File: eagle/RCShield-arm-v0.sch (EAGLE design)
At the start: 48 parts, among them U3 TS5A3157DBV, U4 XBEE, U5 TS5A3157DBV, X1 USB

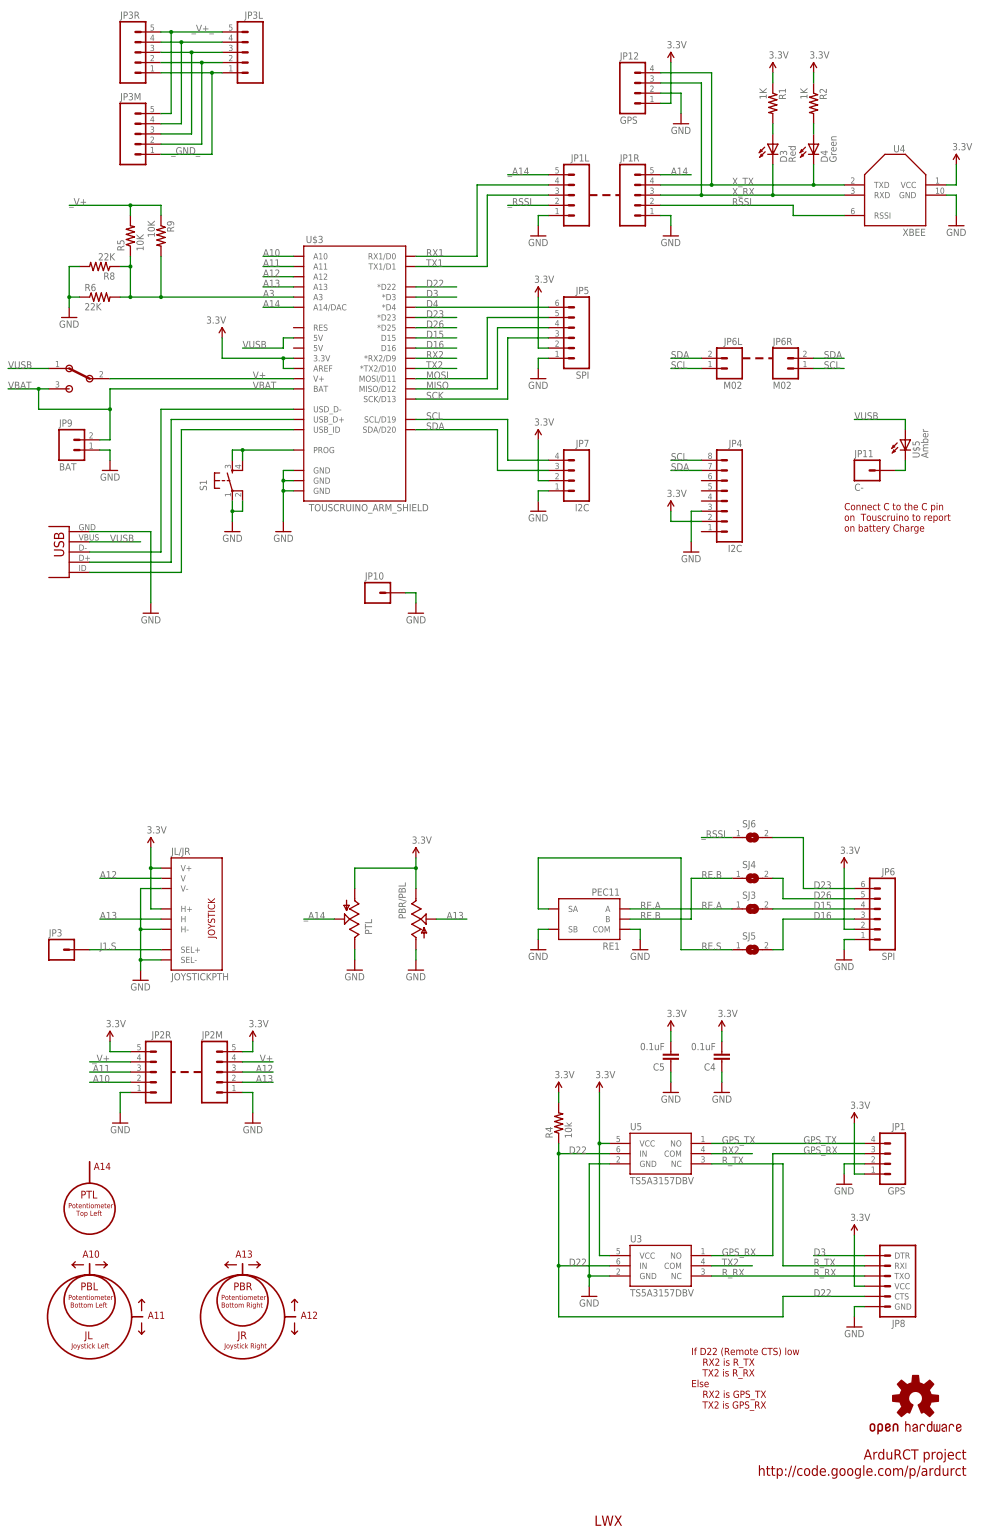
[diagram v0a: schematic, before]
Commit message: 
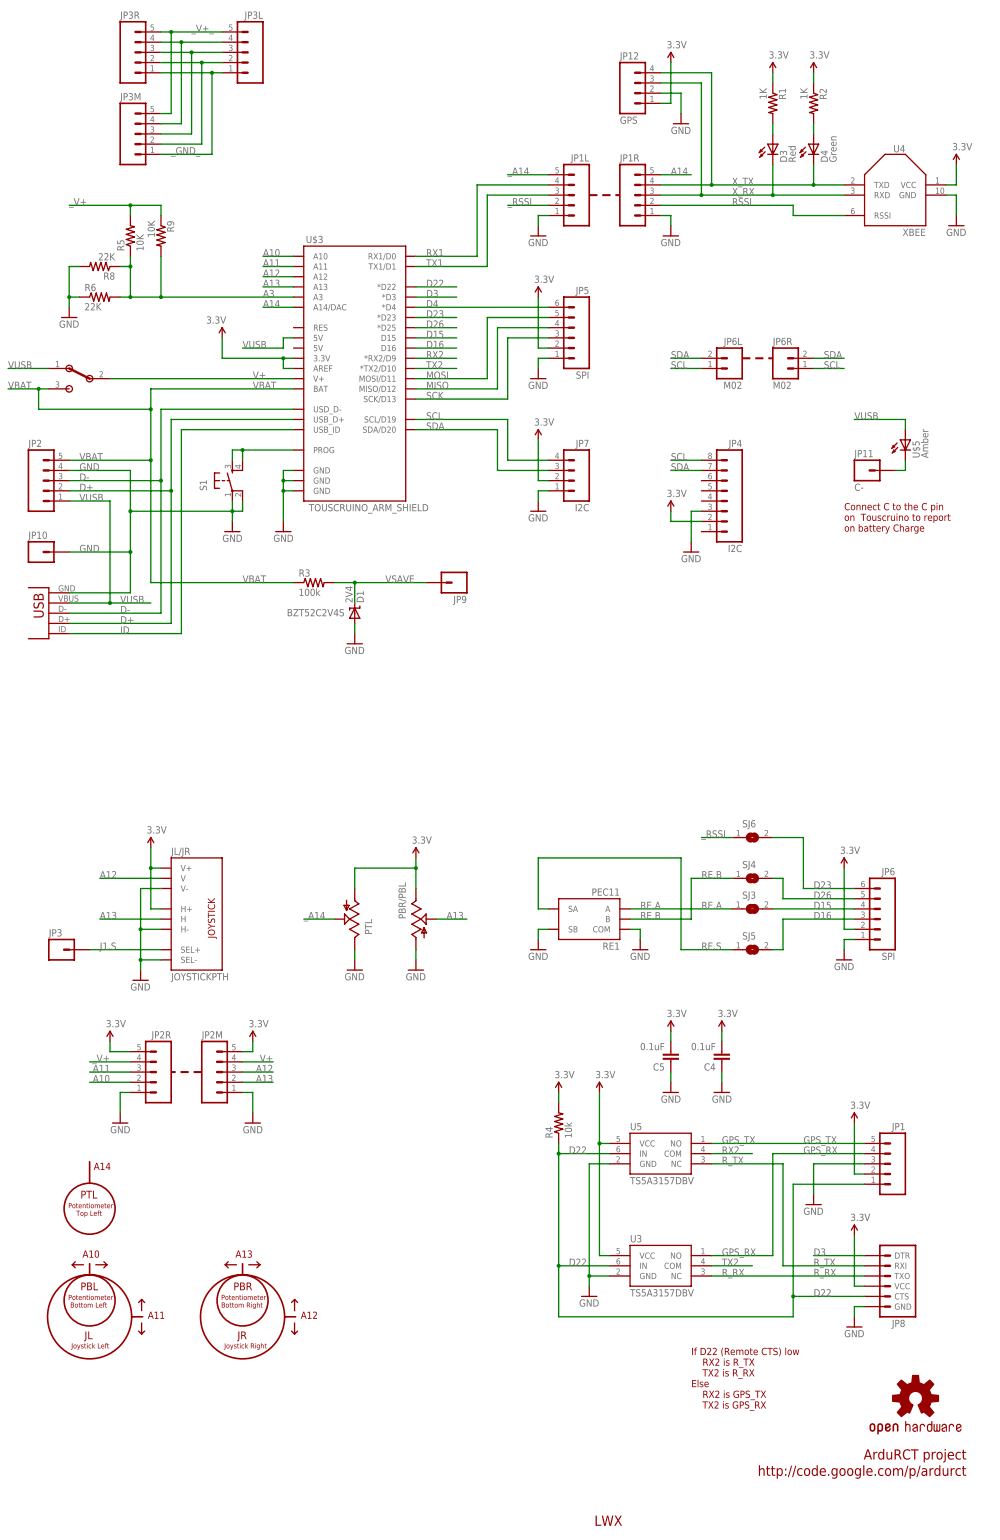
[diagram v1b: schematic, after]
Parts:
- added D1: 2V4, SparkFun:DIODE-ZENER-BZT52
- added JP2: (no value), SparkFun:M05PTH
- added R3: 100k, SparkFun:RESISTOR0805-RES
- JP1: value GPS -> (none); device wibauxl:M04 -> SparkFun:M05PTH
- JP9: value BAT -> M01PTH; device wibauxl:M02 -> SparkFun:M01PTH
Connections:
- net N$9 renamed ID
- removed net N$2: U$3.USD_D-, X1.D-
- removed net N$3: U$3.USB_D+, X1.D+
- new net D+: JP2.2, U$3.USB_D+, X1.D+
- new net D-: JP2.3, U$3.USD_D-, X1.D-
- new net VSAVE: D1.C, JP9.1, R3.2
- net 3.3V: now also JP1.2; no longer JP1.1
- net D22: now also JP1.1
- net GND: now also D1.A, JP1.3, JP2.4; no longer JP1.2, JP9.1
- net GPS_RX: now also JP1.4; no longer JP1.3
- net GPS_TX: now also JP1.5; no longer JP1.4
- net VBAT: now also JP2.5, R3.1; no longer JP9.2
- net VUSB: now also JP2.1
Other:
- note added: "BZT52C2V4S"
- moved on the sheet: JP10
